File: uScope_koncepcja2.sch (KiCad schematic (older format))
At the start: 31 parts

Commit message: - schematic as hierarchical - added cache lib
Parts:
- renumbered V_Focus to V_Focus?, V_K to V_K?, V_Wh to V_Wh?
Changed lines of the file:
@@
 EESchema Schematic File Version 4
+LIBS:uScope-cache
 EELAYER 26 0
 EELAYER END
 $Descr A4 11693 8268
 encoding utf-8
-Sheet 1 1
+Sheet 1 5
 Title ""
 Date "2020-08-14"
@@
 $EndComp
 $Comp
-L pspice:VSOURCE V_K
+L pspice:VSOURCE V_K?
 U 1 1 5F36B478
 P 3350 3550
-F 0 "V_K" H 2984 3504 50  0000 R CNN
+F 0 "V_K?" H 2984 3504 50  0000 R CNN
 F 1 "4.5 kV" H 2984 3595 50  0000 R CNN
 F 2 "" H 3350 3550 50  0001 C CNN
@@
 $EndComp
 $Comp
-L pspice:VSOURCE V_Wh
+L pspice:VSOURCE V_Wh?
 U 1 1 5F36B607
 P 4300 3550
-F 0 "V_Wh" H 3934 3504 50  0000 R CNN
+F 0 "V_Wh?" H 3934 3504 50  0000 R CNN
 F 1 "5 kV" H 3934 3595 50  0000 R CNN
 F 2 "" H 4300 3550 50  0001 C CNN
@@
 $EndComp
 $Comp
-L pspice:VSOURCE V_Focus
+L pspice:VSOURCE V_Focus?
 U 1 1 5F36B645
 P 5450 3550
-F 0 "V_Focus" H 5678 3596 50  0000 L CNN
+F 0 "V_Focus?" H 5678 3596 50  0000 L CNN
 F 1 "500 V" H 5678 3505 50  0000 L CNN
 F 2 "" H 5450 3550 50  0001 C CNN

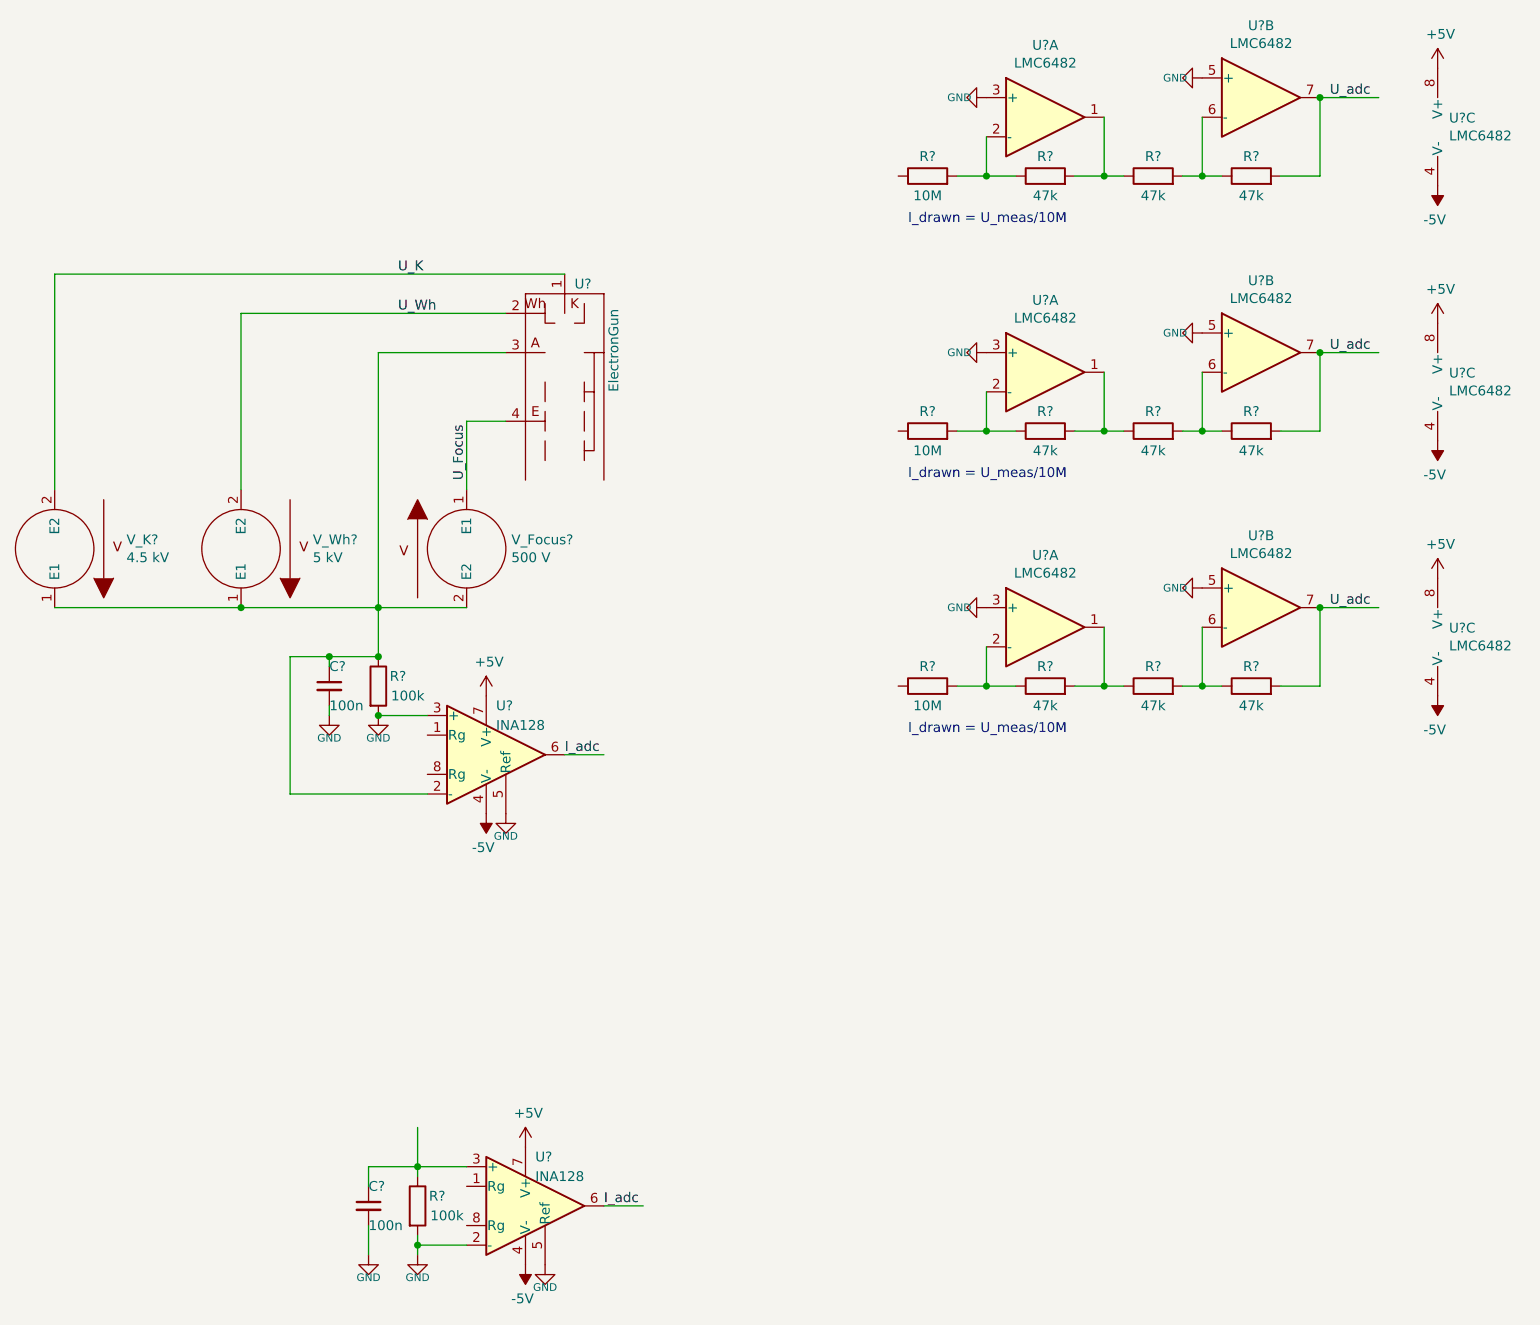
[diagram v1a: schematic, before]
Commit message: - moved voltmeters to separate sheet - hierarchical sheets
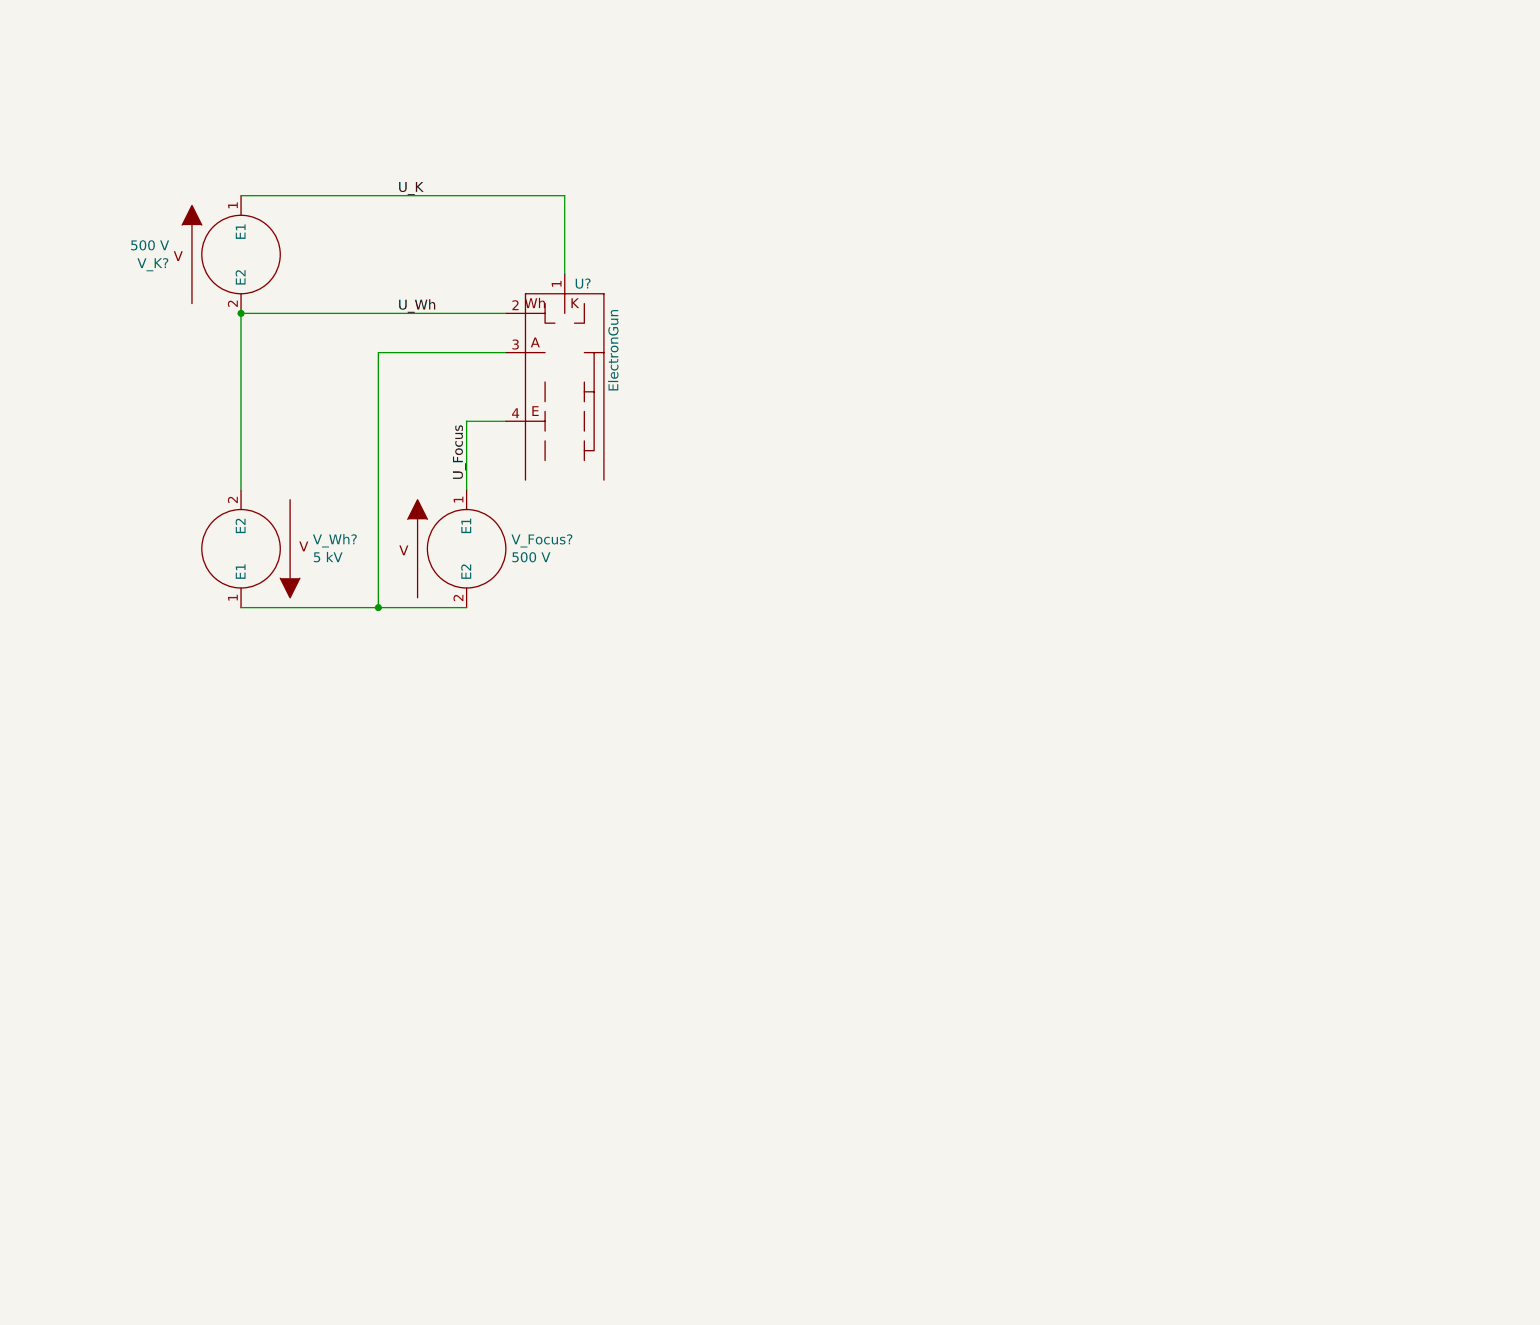
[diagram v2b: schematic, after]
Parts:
- removed C? (x2): 100n, symbol Device:C_Small
- removed R? (x9): 47k, symbol Device:R
- removed R? (x3): 10M, symbol Device:R
- removed R? (x2): 100k, symbol Device:R
- removed U? (x9): LMC6482, symbol Amplifier_Operational:LMC6482
- removed U? (x2): INA128, symbol Amplifier_Instrumentation:INA128
- V_K?: value 4.5 kV -> 500 V
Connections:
- net labels removed: +5V, -5V, GND, I_adc, U_adc
- wire segments 66 -> 10
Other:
- note removed: "I_drawn = U_meas/10M"
- moved on the sheet: V_K?

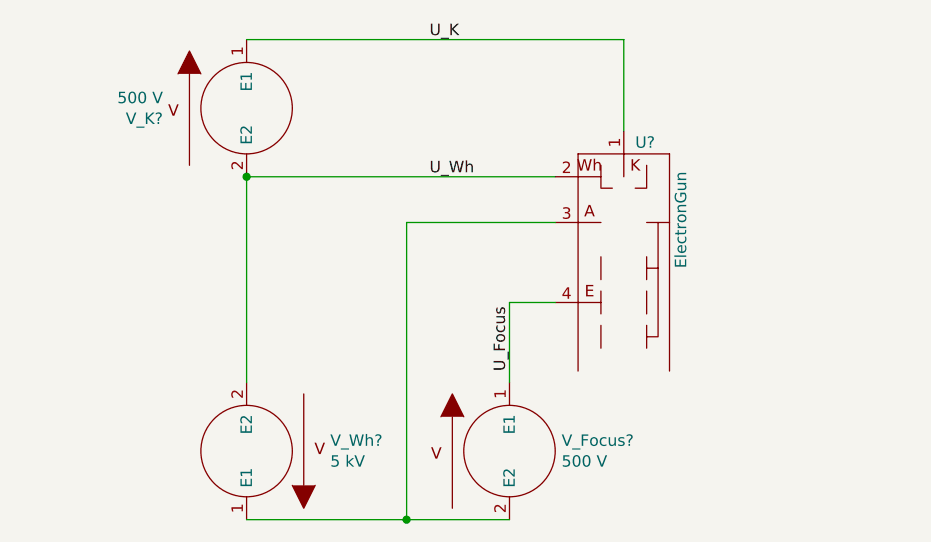
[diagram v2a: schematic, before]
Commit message: - added DC/DC converter to library, - moved ammeter & drivers to sub-sheet, - further develop
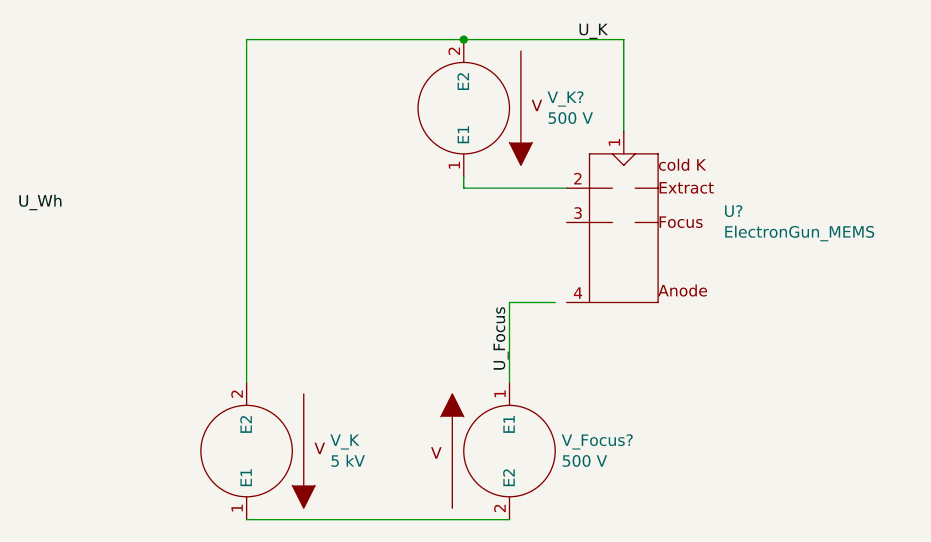
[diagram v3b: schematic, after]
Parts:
- removed U?: ElectronGun, symbol uScope:ElectronGun
- added U?: ElectronGun_MEMS, symbol uScope:ElectronGun_MEMS
- gave numbers to parts that had none: 1
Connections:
- wire segments 10 -> 9
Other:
- moved on the sheet: V_K?
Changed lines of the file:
@@
 $Descr A4 11693 8268
 encoding utf-8
-Sheet 4 7
+Sheet 4 8
 Title ""
 Date "2020-08-14"
@@
 $EndDescr
 $Comp
-L uScope:ElectronGun U?
-U 1 1 5F36B27A
-P 5950 2700
-F 0 "U?" H 6000 3200 50  0000 L CNN
-F 1 "ElectronGun" V 6200 2650 50  0000 L CNN
-F 2 "" H 5950 2200 50  0001 C CNN
-F 3 "" H 5950 2200 50  0001 C CNN
-	1    5950 2700
-	1    0    0    -1
+L pspice:VSOURCE V_K?
+U 1 1 5F36B478
+P 5250 2050
+F 0 "V_K?" H 4884 2004 50  0000 R CNN
+F 1 "500 V" H 4884 2095 50  0000 R CNN
+F 2 "" H 5250 2050 50  0001 C CNN
+F 3 "~" H 5250 2050 50  0001 C CNN
+	1    5250 2050
+	-1   0    0    1
 $EndComp
 $Comp
-L pspice:VSOURCE V_K?
-U 1 1 5F36B478
-P 4300 2050
-F 0 "V_K?" H 3934 2004 50  0000 R CNN
-F 1 "500 V" H 3934 2095 50  0000 R CNN
-F 2 "" H 4300 2050 50  0001 C CNN
-F 3 "~" H 4300 2050 50  0001 C CNN
-	1    4300 2050
-	1    0    0    -1
-$EndComp
-$Comp
-L pspice:VSOURCE V_Wh?
+L pspice:VSOURCE V_K
 U 1 1 5F36B607
 P 4300 3550
-F 0 "V_Wh?" H 3934 3504 50  0000 R CNN
+F 0 "V_K" H 3934 3504 50  0000 R CNN
 F 1 "5 kV" H 3934 3595 50  0000 R CNN
 F 2 "" H 4300 3550 50  0001 C CNN
@@
 	5450 2900 5450 3250
 Wire Wire Line
-	5650 2350 4300 2350
-Wire Wire Line
-	4300 2350 4300 3250
+	4300 1750 4300 3250
 Wire Wire Line
 	5650 2900 5450 2900
-Wire Wire Line
-	5650 2550 5000 2550
-Wire Wire Line
-	5000 2550 5000 3850
-Wire Wire Line
-	5000 3850 5450 3850
-Connection ~ 5000 3850
-Wire Wire Line
-	4300 3850 5000 3850
-Text Label 5100 1750 0    50   ~ 0
+Text Label 5750 1750 0    50   ~ 0
 U_K
-Text Label 5100 2350 0    50   ~ 0
+Text Label 3300 2500 0    50   ~ 0
 U_Wh
 Text Label 5450 3200 1    50   ~ 0
 U_Focus
 Wire Wire Line
-	4300 1750 5950 1750
-Connection ~ 4300 2350
+	4300 1750 5250 1750
 Wire Wire Line
 	5950 1750 5950 2150
+$Comp
+L uScope:ElectronGun_MEMS U?
+U 1 1 5F60370C
+P 5950 2700
+F 0 "U?" H 6387 2898 50  0000 L CNN
+F 1 "ElectronGun_MEMS" H 6387 2807 50  0000 L CNN
+F 2 "" H 5950 2200 50  0001 C CNN
+F 3 "" H 5950 2200 50  0001 C CNN
+	1    5950 2700
+	1    0    0    -1
+$EndComp
+Wire Wire Line
+	4300 3850 5450 3850
+Connection ~ 5250 1750
+Wire Wire Line
+	5250 1750 5950 1750
+Wire Wire Line
+	5700 2400 5250 2400
+Wire Wire Line
+	5250 2400 5250 2350
 $EndSCHEMATC
